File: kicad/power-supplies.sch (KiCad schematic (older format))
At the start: 28 parts, among them J2 BARREL_JACK, Q4 MMBT3906WT1G, Q5 FDG6301N_F085, U3 AP3211, U7 TL431

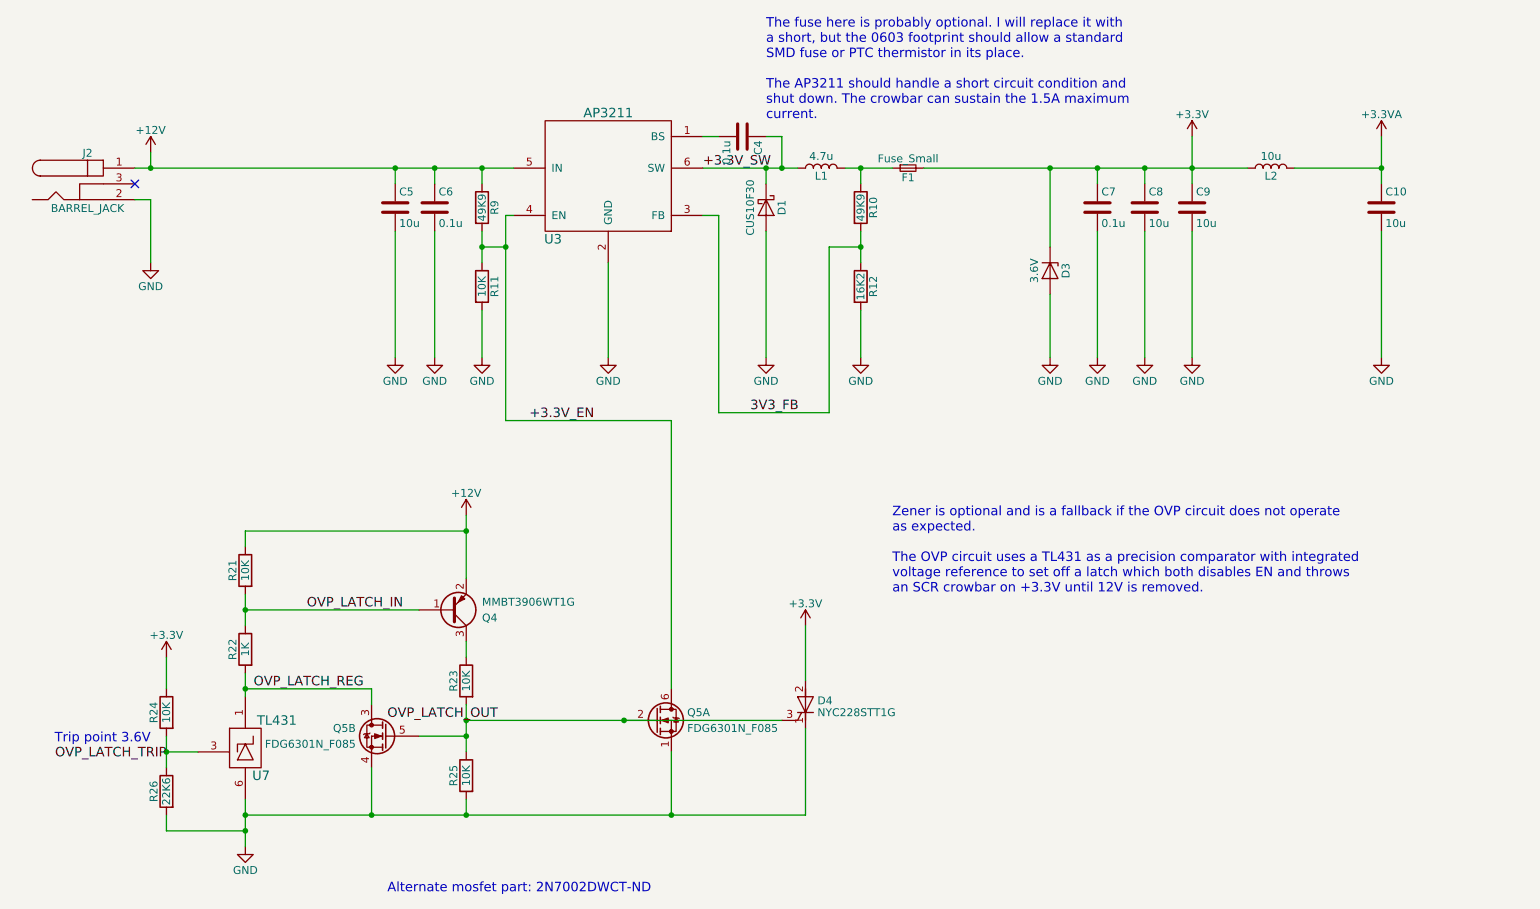
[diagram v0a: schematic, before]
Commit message: Finished placement of all parts. Routed power supply.
The board has been shrunk by 10mm or so. The elimination of the giant
directional switch is the reason this is even possible.
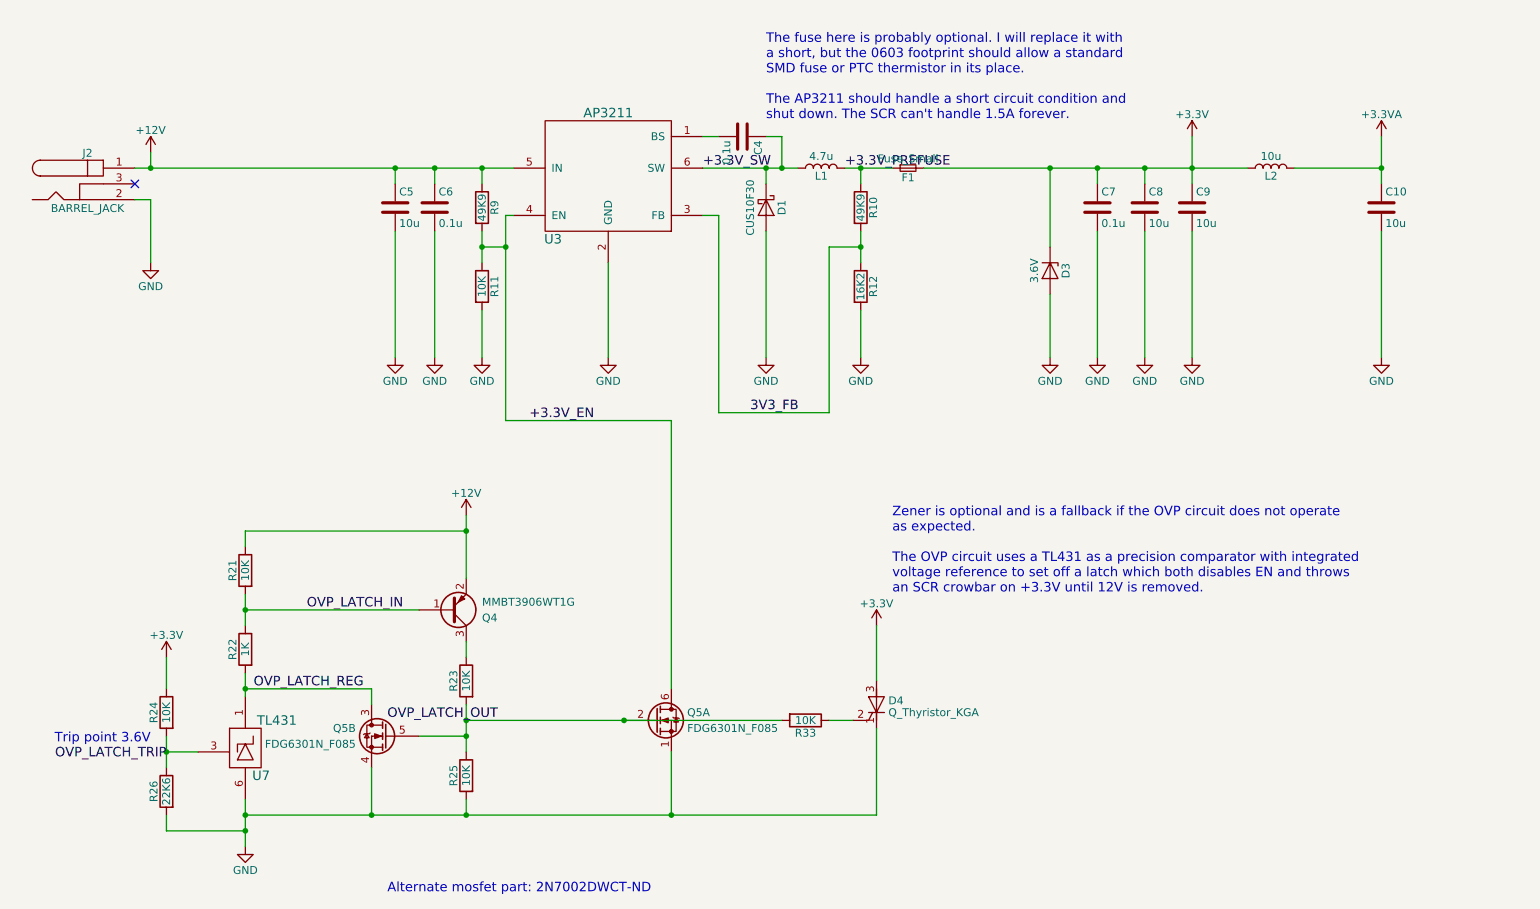
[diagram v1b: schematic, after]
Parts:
- removed D4: NYC228STT1G, TO_SOT_Packages_SMD:SOT-223-3Lead_TabPin2, symbol Q_Thyristor_KAG
- added D4: Q_Thyristor_KGA, TO_SOT_Packages_SMD:SOT-23, symbol Q_Thyristor_KGA
- added R33: 10K, Resistors_SMD:R_0402, symbol R
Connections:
- net +3V3: now also D4.3 (A)
- net GND: now also D4.1 (K)
- net OVP_LATCH_OUT: now also R33.2
- net +3.3V_PREFUSE: now reaches F1.1, L1.2, R10.1
- new net: D4.2 (G), R33.1
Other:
- note added: "The fuse here is probably optional. I will replace it with\na short, but the 0603 footprint should allow a standard\nSMD fuse or PTC thermistor in its place.\n\nThe AP3211 should handle a short circuit condition and\nshut down. The SCR can't handle 1.5A forever."
- note removed: "The fuse here is probably optional. I will replace it with\na short, but the 0603 footprint should allow a standard\nSMD fuse or PTC thermistor in its place.\n\nThe AP3211 should handle a short circuit condition and\nshut down. The crowbar can sustain the 1.5A maximum\ncurrent."
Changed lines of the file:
@@
 $EndComp
 $Comp
-L GND #PWR26
+L GND #PWR023
 U 1 1 592084EC
 P 1600 2100
-F 0 "#PWR26" H 1600 1850 50  0001 C CNN
+F 0 "#PWR023" H 1600 1850 50  0001 C CNN
 F 1 "GND" H 1600 1950 50  0000 C CNN
 F 2 "" H 1600 2100 50  0001 C CNN
@@
 $EndComp
 $Comp
-L +12V #PWR25
+L +12V #PWR024
 U 1 1 59208505
 P 1600 1400
-F 0 "#PWR25" H 1600 1250 50  0001 C CNN
+F 0 "#PWR024" H 1600 1250 50  0001 C CNN
 F 1 "+12V" H 1600 1540 50  0000 C CNN
 F 2 "" H 1600 1400 50  0001 C CNN
@@
 $EndComp
 $Comp
-L GND #PWR31
+L GND #PWR025
 U 1 1 592088C5
 P 5500 2700
-F 0 "#PWR31" H 5500 2450 50  0001 C CNN
+F 0 "#PWR025" H 5500 2450 50  0001 C CNN
 F 1 "GND" H 5500 2550 50  0000 C CNN
 F 2 "" H 5500 2700 50  0001 C CNN
@@
 $EndComp
 $Comp
-L GND #PWR30
+L GND #PWR026
 U 1 1 59208941
 P 4500 2700
-F 0 "#PWR30" H 4500 2450 50  0001 C CNN
+F 0 "#PWR026" H 4500 2450 50  0001 C CNN
 F 1 "GND" H 4500 2550 50  0000 C CNN
 F 2 "" H 4500 2700 50  0001 C CNN
@@
 $EndComp
 $Comp
-L +3.3V #PWR23
+L +3.3V #PWR027
 U 1 1 59208C89
 P 8200 1300
-F 0 "#PWR23" H 8200 1150 50  0001 C CNN
+F 0 "#PWR027" H 8200 1150 50  0001 C CNN
 F 1 "+3.3V" H 8200 1440 50  0000 C CNN
 F 2 "" H 8200 1300 50  0001 C CNN
@@
 $EndComp
 $Comp
-L GND #PWR36
+L GND #PWR028
 U 1 1 59208D24
 P 8200 2700
-F 0 "#PWR36" H 8200 2450 50  0001 C CNN
+F 0 "#PWR028" H 8200 2450 50  0001 C CNN
 F 1 "GND" H 8200 2550 50  0000 C CNN
 F 2 "" H 8200 2700 50  0001 C CNN
@@
 $EndComp
 $Comp
-L GND #PWR27
+L GND #PWR029
 U 1 1 59208EA1
 P 3150 2700
-F 0 "#PWR27" H 3150 2450 50  0001 C CNN
+F 0 "#PWR029" H 3150 2450 50  0001 C CNN
 F 1 "GND" H 3150 2550 50  0000 C CNN
 F 2 "" H 3150 2700 50  0001 C CNN
@@
 $EndComp
 $Comp
-L GND #PWR34
+L GND #PWR030
 U 1 1 5920907B
 P 7600 2700
-F 0 "#PWR34" H 7600 2450 50  0001 C CNN
+F 0 "#PWR030" H 7600 2450 50  0001 C CNN
 F 1 "GND" H 7600 2550 50  0000 C CNN
 F 2 "" H 7600 2700 50  0001 C CNN
@@
 $EndComp
 $Comp
-L GND #PWR28
+L GND #PWR031
 U 1 1 592091A5
 P 3400 2700
-F 0 "#PWR28" H 3400 2450 50  0001 C CNN
+F 0 "#PWR031" H 3400 2450 50  0001 C CNN
 F 1 "GND" H 3400 2550 50  0000 C CNN
 F 2 "" H 3400 2700 50  0001 C CNN
@@
 $EndComp
 $Comp
-L GND #PWR32
+L GND #PWR032
 U 1 1 592093A2
 P 6100 2700
-F 0 "#PWR32" H 6100 2450 50  0001 C CNN
+F 0 "#PWR032" H 6100 2450 50  0001 C CNN
 F 1 "GND" H 6100 2550 50  0000 C CNN
 F 2 "" H 6100 2700 50  0001 C CNN
@@
 $EndComp
 $Comp
-L GND #PWR29
+L GND #PWR033
 U 1 1 59209C78
 P 3700 2700
-F 0 "#PWR29" H 3700 2450 50  0001 C CNN
+F 0 "#PWR033" H 3700 2450 50  0001 C CNN
 F 1 "GND" H 3700 2550 50  0000 C CNN
 F 2 "" H 3700 2700 50  0001 C CNN
@@
 $EndComp
 $Comp
-L GND #PWR35
+L GND #PWR034
 U 1 1 5920A4A0
 P 7900 2700
-F 0 "#PWR35" H 7900 2450 50  0001 C CNN
+F 0 "#PWR034" H 7900 2450 50  0001 C CNN
 F 1 "GND" H 7900 2550 50  0000 C CNN
 F 2 "" H 7900 2700 50  0001 C CNN
@@
 $EndComp
 $Comp
-L GND #PWR37
+L GND #PWR035
 U 1 1 592C8FE8
 P 9400 2700
-F 0 "#PWR37" H 9400 2450 50  0001 C CNN
+F 0 "#PWR035" H 9400 2450 50  0001 C CNN
 F 1 "GND" H 9400 2550 50  0000 C CNN
 F 2 "" H 9400 2700 50  0001 C CNN
@@
 $EndComp
 $Comp
-L +3.3VA #PWR24
+L +3.3VA #PWR036
 U 1 1 592C9106
 P 9400 1300
-F 0 "#PWR24" H 9400 1150 50  0001 C CNN
+F 0 "#PWR036" H 9400 1150 50  0001 C CNN
 F 1 "+3.3VA" H 9400 1440 50  0000 C CNN
 F 2 "" H 9400 1300 50  0001 C CNN
@@
 $EndComp
 $Comp
-L GND #PWR33
+L GND #PWR037
 U 1 1 5987D189
 P 7300 2700
-F 0 "#PWR33" H 7300 2450 50  0001 C CNN
+F 0 "#PWR037" H 7300 2450 50  0001 C CNN
 F 1 "GND" H 7300 2550 50  0000 C CNN
 F 2 "" H 7300 2700 50  0001 C CNN
@@
 $EndComp
 $Comp
-L GND #PWR41
+L GND #PWR038
 U 1 1 5998FEAD
 P 2200 5800
-F 0 "#PWR41" H 2200 5550 50  0001 C CNN
+F 0 "#PWR038" H 2200 5550 50  0001 C CNN
 F 1 "GND" H 2200 5650 50  0000 C CNN
 F 2 "" H 2200 5800 50  0001 C CNN
@@
 Trip point 3.6V
 $Comp
-L +12V #PWR38
+L +12V #PWR039
 U 1 1 599906B9
 P 3600 3700
-F 0 "#PWR38" H 3600 3550 50  0001 C CNN
+F 0 "#PWR039" H 3600 3550 50  0001 C CNN
 F 1 "+12V" H 3600 3840 50  0000 C CNN
 F 2 "" H 3600 3700 50  0001 C CNN
@@
 $EndComp
 $Comp
-L +3.3V #PWR40
+L +3.3V #PWR040
 U 1 1 59991F79
 P 1700 4600
-F 0 "#PWR40" H 1700 4450 50  0001 C CNN
+F 0 "#PWR040" H 1700 4450 50  0001 C CNN
 F 1 "+3.3V" H 1700 4740 50  0000 C CNN
 F 2 "" H 1700 4600 50  0001 C CNN
@@
 Connection ~ 2200 4300
 Wire Wire Line
-	2200 5600 5750 5600
+	2200 5600 6200 5600
 Wire Wire Line
 	3600 5600 3600 5500
@@
 	4900 5600 4900 5200
 Connection ~ 3600 5600
-Wire Wire Line
-	3600 5000 5600 5000
 Connection ~ 3600 5000
 Wire Wire Line
@@
 	3000 4900 3000 4800
 $Comp
-L Q_Thyristor_KAG D4
-U 1 1 59997C41
-P 5750 4900
-F 0 "D4" H 5825 4925 50  0000 L CNN
-F 1 "NYC228STT1G" H 5825 4850 50  0000 L CNN
-F 2 "TO_SOT_Packages_SMD:SOT-223-3Lead_TabPin2" V 5750 4900 50  0001 C CNN
-F 3 "" V 5750 4900 50  0001 C CNN
-F 4 "NYC228STT1GOSCT-ND" H 5750 4900 60  0001 C CNN "Part No."
-	1    5750 4900
-	1    0    0    -1
-$EndComp
-$Comp
-L +3.3V #PWR39
+L +3.3V #PWR041
 U 1 1 599981D4
-P 5750 4400
-F 0 "#PWR39" H 5750 4250 50  0001 C CNN
-F 1 "+3.3V" H 5750 4540 50  0000 C CNN
-F 2 "" H 5750 4400 50  0001 C CNN
-F 3 "" H 5750 4400 50  0001 C CNN
-	1    5750 4400
-	1    0    0    -1
-$EndComp
-Wire Wire Line
-	5750 4400 5750 4750
+P 6200 4400
+F 0 "#PWR041" H 6200 4250 50  0001 C CNN
+F 1 "+3.3V" H 6200 4540 50  0000 C CNN
+F 2 "" H 6200 4400 50  0001 C CNN
+F 3 "" H 6200 4400 50  0001 C CNN
+	1    6200 4400
+	1    0    0    -1
+$EndComp
+Wire Wire Line
+	6200 4400 6200 4750
 Wire Wire Line
 	3850 1800 3850 3100
@@
 +3.3V_EN
 Wire Wire Line
-	5750 5600 5750 5050
+	6200 5600 6200 5050
 Connection ~ 4900 5600
 Connection ~ 4600 5000
@@
 	6500 1500 8550 1500
 Text Notes 5500 1200 0    60   ~ 0
-The fuse here is probably optional. I will replace it with\na short, but the 0603 footprint should allow a standard\nSMD fuse or PTC thermistor in its place.\n\nThe AP3211 should handle a short circuit condition and\nshut down. The crowbar can sustain the 1.5A maximum\ncurrent.
+The fuse here is probably optional. I will replace it with\na short, but the 0603 footprint should allow a standard\nSMD fuse or PTC thermistor in its place.\n\nThe AP3211 should handle a short circuit condition and\nshut down. The SCR can't handle 1.5A forever.
+$Comp
+L R R33
+U 1 1 59AB54BD
+P 5750 5000
+F 0 "R33" V 5830 5000 50  0000 C CNN
+F 1 "10K" V 5750 5000 50  0000 C CNN
+F 2 "Resistors_SMD:R_0402" V 5680 5000 50  0001 C CNN
+F 3 "" H 5750 5000 50  0001 C CNN
+F 4 "311-10.0KLRCT-ND" H 5750 5000 60  0001 C CNN "Part No."
+	1    5750 5000
+	0    1    1    0
+$EndComp
+Wire Wire Line
+	3600 5000 5600 5000
+Wire Wire Line
+	5900 5000 6050 5000
+$Comp
+L Q_Thyristor_KGA D4
+U 1 1 59ACE5D6
+P 6200 4900
+F 0 "D4" H 6275 4925 50  0000 L CNN
+F 1 "Q_Thyristor_KGA" H 6275 4850 50  0000 L CNN
+F 2 "TO_SOT_Packages_SMD:SOT-23" V 6200 4900 50  0001 C CNN
+F 3 "" V 6200 4900 50  0001 C CNN
+F 4 "NYC0102BLT1G" H 6200 4900 60  0001 C CNN "Part No."
+	1    6200 4900
+	1    0    0    -1
+$EndComp
+Text Label 6000 1500 0    60   ~ 0
++3.3V_PREFUSE
 $EndSCHEMATC

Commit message: Fixed some capacitor footprints
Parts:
- D4: Part No. NYC0102BLT1G -> NYC0102BLT1GOSCT-ND
- R26: Part No. (none) -> YAG3061CT-ND
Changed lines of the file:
@@
 $EndComp
 $Comp
-L GND #PWR023
+L GND #PWR024
 U 1 1 592084EC
 P 1600 2100
-F 0 "#PWR023" H 1600 1850 50  0001 C CNN
+F 0 "#PWR024" H 1600 1850 50  0001 C CNN
 F 1 "GND" H 1600 1950 50  0000 C CNN
 F 2 "" H 1600 2100 50  0001 C CNN
@@
 $EndComp
 $Comp
-L +12V #PWR024
+L +12V #PWR025
 U 1 1 59208505
 P 1600 1400
-F 0 "#PWR024" H 1600 1250 50  0001 C CNN
+F 0 "#PWR025" H 1600 1250 50  0001 C CNN
 F 1 "+12V" H 1600 1540 50  0000 C CNN
 F 2 "" H 1600 1400 50  0001 C CNN
@@
 $EndComp
 $Comp
-L GND #PWR025
+L GND #PWR026
 U 1 1 592088C5
 P 5500 2700
-F 0 "#PWR025" H 5500 2450 50  0001 C CNN
+F 0 "#PWR026" H 5500 2450 50  0001 C CNN
 F 1 "GND" H 5500 2550 50  0000 C CNN
 F 2 "" H 5500 2700 50  0001 C CNN
@@
 $EndComp
 $Comp
-L GND #PWR026
+L GND #PWR027
 U 1 1 59208941
 P 4500 2700
-F 0 "#PWR026" H 4500 2450 50  0001 C CNN
+F 0 "#PWR027" H 4500 2450 50  0001 C CNN
 F 1 "GND" H 4500 2550 50  0000 C CNN
 F 2 "" H 4500 2700 50  0001 C CNN
@@
 $EndComp
 $Comp
-L +3.3V #PWR027
+L +3.3V #PWR028
 U 1 1 59208C89
 P 8200 1300
-F 0 "#PWR027" H 8200 1150 50  0001 C CNN
+F 0 "#PWR028" H 8200 1150 50  0001 C CNN
 F 1 "+3.3V" H 8200 1440 50  0000 C CNN
 F 2 "" H 8200 1300 50  0001 C CNN
@@
 $EndComp
 $Comp
-L GND #PWR028
+L GND #PWR029
 U 1 1 59208D24
 P 8200 2700
-F 0 "#PWR028" H 8200 2450 50  0001 C CNN
+F 0 "#PWR029" H 8200 2450 50  0001 C CNN
 F 1 "GND" H 8200 2550 50  0000 C CNN
 F 2 "" H 8200 2700 50  0001 C CNN
@@
 $EndComp
 $Comp
-L GND #PWR029
+L GND #PWR030
 U 1 1 59208EA1
 P 3150 2700
-F 0 "#PWR029" H 3150 2450 50  0001 C CNN
+F 0 "#PWR030" H 3150 2450 50  0001 C CNN
 F 1 "GND" H 3150 2550 50  0000 C CNN
 F 2 "" H 3150 2700 50  0001 C CNN
@@
 $EndComp
 $Comp
-L GND #PWR030
+L GND #PWR031
 U 1 1 5920907B
 P 7600 2700
-F 0 "#PWR030" H 7600 2450 50  0001 C CNN
+F 0 "#PWR031" H 7600 2450 50  0001 C CNN
 F 1 "GND" H 7600 2550 50  0000 C CNN
 F 2 "" H 7600 2700 50  0001 C CNN
@@
 $EndComp
 $Comp
-L GND #PWR031
+L GND #PWR032
 U 1 1 592091A5
 P 3400 2700
-F 0 "#PWR031" H 3400 2450 50  0001 C CNN
+F 0 "#PWR032" H 3400 2450 50  0001 C CNN
 F 1 "GND" H 3400 2550 50  0000 C CNN
 F 2 "" H 3400 2700 50  0001 C CNN
@@
 $EndComp
 $Comp
-L GND #PWR032
+L GND #PWR033
 U 1 1 592093A2
 P 6100 2700
-F 0 "#PWR032" H 6100 2450 50  0001 C CNN
+F 0 "#PWR033" H 6100 2450 50  0001 C CNN
 F 1 "GND" H 6100 2550 50  0000 C CNN
 F 2 "" H 6100 2700 50  0001 C CNN
@@
 $EndComp
 $Comp
-L GND #PWR033
+L GND #PWR034
 U 1 1 59209C78
 P 3700 2700
-F 0 "#PWR033" H 3700 2450 50  0001 C CNN
+F 0 "#PWR034" H 3700 2450 50  0001 C CNN
 F 1 "GND" H 3700 2550 50  0000 C CNN
 F 2 "" H 3700 2700 50  0001 C CNN
@@
 $EndComp
 $Comp
-L GND #PWR034
+L GND #PWR035
 U 1 1 5920A4A0
 P 7900 2700
-F 0 "#PWR034" H 7900 2450 50  0001 C CNN
+F 0 "#PWR035" H 7900 2450 50  0001 C CNN
 F 1 "GND" H 7900 2550 50  0000 C CNN
 F 2 "" H 7900 2700 50  0001 C CNN
@@
 $EndComp
 $Comp
-L GND #PWR035
+L GND #PWR036
 U 1 1 592C8FE8
 P 9400 2700
-F 0 "#PWR035" H 9400 2450 50  0001 C CNN
+F 0 "#PWR036" H 9400 2450 50  0001 C CNN
 F 1 "GND" H 9400 2550 50  0000 C CNN
 F 2 "" H 9400 2700 50  0001 C CNN
@@
 $EndComp
 $Comp
-L +3.3VA #PWR036
+L +3.3VA #PWR037
 U 1 1 592C9106
 P 9400 1300
-F 0 "#PWR036" H 9400 1150 50  0001 C CNN
+F 0 "#PWR037" H 9400 1150 50  0001 C CNN
 F 1 "+3.3VA" H 9400 1440 50  0000 C CNN
 F 2 "" H 9400 1300 50  0001 C CNN
@@
 $EndComp
 $Comp
-L GND #PWR037
+L GND #PWR038
 U 1 1 5987D189
 P 7300 2700
-F 0 "#PWR037" H 7300 2450 50  0001 C CNN
+F 0 "#PWR038" H 7300 2450 50  0001 C CNN
 F 1 "GND" H 7300 2550 50  0000 C CNN
 F 2 "" H 7300 2700 50  0001 C CNN
@@
 F 2 "Resistors_SMD:R_0402" V 1630 5450 50  0001 C CNN
 F 3 "" H 1700 5450 50  0001 C CNN
+F 4 "YAG3061CT-ND" H 1700 5450 60  0001 C CNN "Part No."
 	1    1700 5450
 	-1   0    0    -1
@@
 $EndComp
 $Comp
-L GND #PWR038
+L GND #PWR039
 U 1 1 5998FEAD
 P 2200 5800
-F 0 "#PWR038" H 2200 5550 50  0001 C CNN
+F 0 "#PWR039" H 2200 5550 50  0001 C CNN
 F 1 "GND" H 2200 5650 50  0000 C CNN
 F 2 "" H 2200 5800 50  0001 C CNN
@@
 Trip point 3.6V
 $Comp
-L +12V #PWR039
+L +12V #PWR040
 U 1 1 599906B9
 P 3600 3700
-F 0 "#PWR039" H 3600 3550 50  0001 C CNN
+F 0 "#PWR040" H 3600 3550 50  0001 C CNN
 F 1 "+12V" H 3600 3840 50  0000 C CNN
 F 2 "" H 3600 3700 50  0001 C CNN
@@
 $EndComp
 $Comp
-L +3.3V #PWR040
+L +3.3V #PWR041
 U 1 1 59991F79
 P 1700 4600
-F 0 "#PWR040" H 1700 4450 50  0001 C CNN
+F 0 "#PWR041" H 1700 4450 50  0001 C CNN
 F 1 "+3.3V" H 1700 4740 50  0000 C CNN
 F 2 "" H 1700 4600 50  0001 C CNN
@@
 	3000 4900 3000 4800
 $Comp
-L +3.3V #PWR041
+L +3.3V #PWR042
 U 1 1 599981D4
 P 6200 4400
-F 0 "#PWR041" H 6200 4250 50  0001 C CNN
+F 0 "#PWR042" H 6200 4250 50  0001 C CNN
 F 1 "+3.3V" H 6200 4540 50  0000 C CNN
 F 2 "" H 6200 4400 50  0001 C CNN
@@
 F 2 "TO_SOT_Packages_SMD:SOT-23" V 6200 4900 50  0001 C CNN
 F 3 "" V 6200 4900 50  0001 C CNN
-F 4 "NYC0102BLT1G" H 6200 4900 60  0001 C CNN "Part No."
+F 4 "NYC0102BLT1GOSCT-ND" H 6200 4900 60  0001 C CNN "Part No."
 	1    6200 4900
 	1    0    0    -1

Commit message: Updated parts for rev B parts order, updated dates
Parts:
- Q5: Part No. FDG6301N_F085CT-ND -> FDG6301N-F085CT-ND
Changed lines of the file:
@@
 Sheet 3 4
 Title "RT Soldering Iron"
-Date "2017-06-02"
-Rev "A"
+Date "2017-11-06"
+Rev "B"
 Comp "Kevin Cuzner"
 Comment1 ""
@@
 F 2 "TO_SOT_Packages_SMD:SOT-363_SC-70-6" H 3300 5200 50  0001 C CNN
 F 3 "" H 3100 5100 50  0001 C CNN
-F 4 "FDG6301N_F085CT-ND" H 3100 5100 60  0001 C CNN "Part No."
+F 4 "FDG6301N-F085CT-ND" H 3100 5100 60  0001 C CNN "Part No."
 	2    3100 5100
 	-1   0    0    -1
@@
 F 2 "TO_SOT_Packages_SMD:SOT-363_SC-70-6" H 5000 5100 50  0001 C CNN
 F 3 "" H 4800 5000 50  0001 C CNN
-F 4 "FDG6301N_F085CT-ND" H 4800 5000 60  0001 C CNN "Part No."
+F 4 "FDG6301N-F085CT-ND" H 4800 5000 60  0001 C CNN "Part No."
 	1    4800 5000
 	1    0    0    -1
